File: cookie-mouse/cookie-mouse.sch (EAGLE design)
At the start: 8 parts

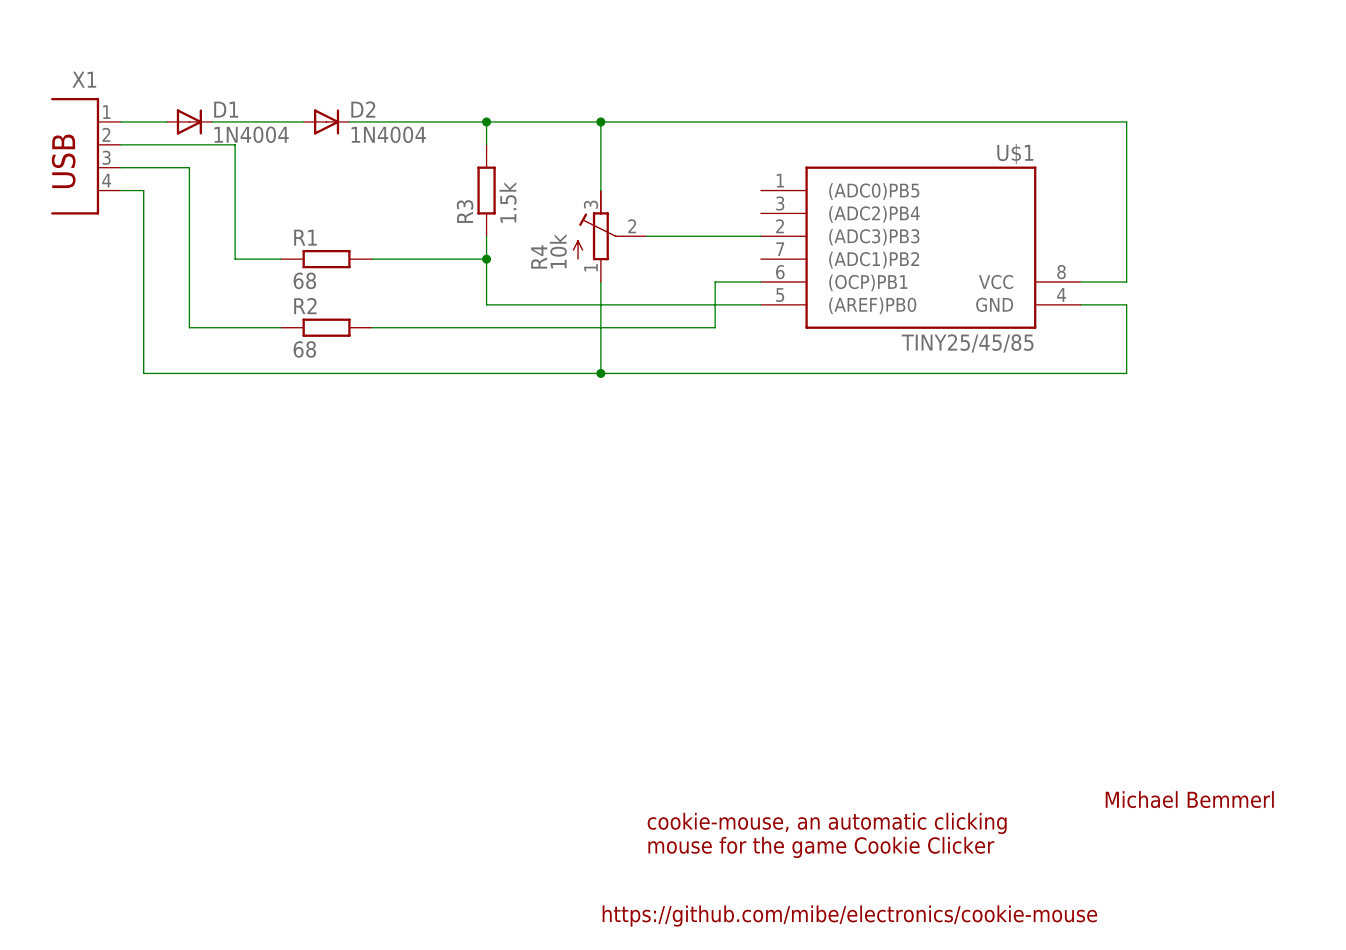
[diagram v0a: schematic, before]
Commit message: Added switch and push button, connected to ground.
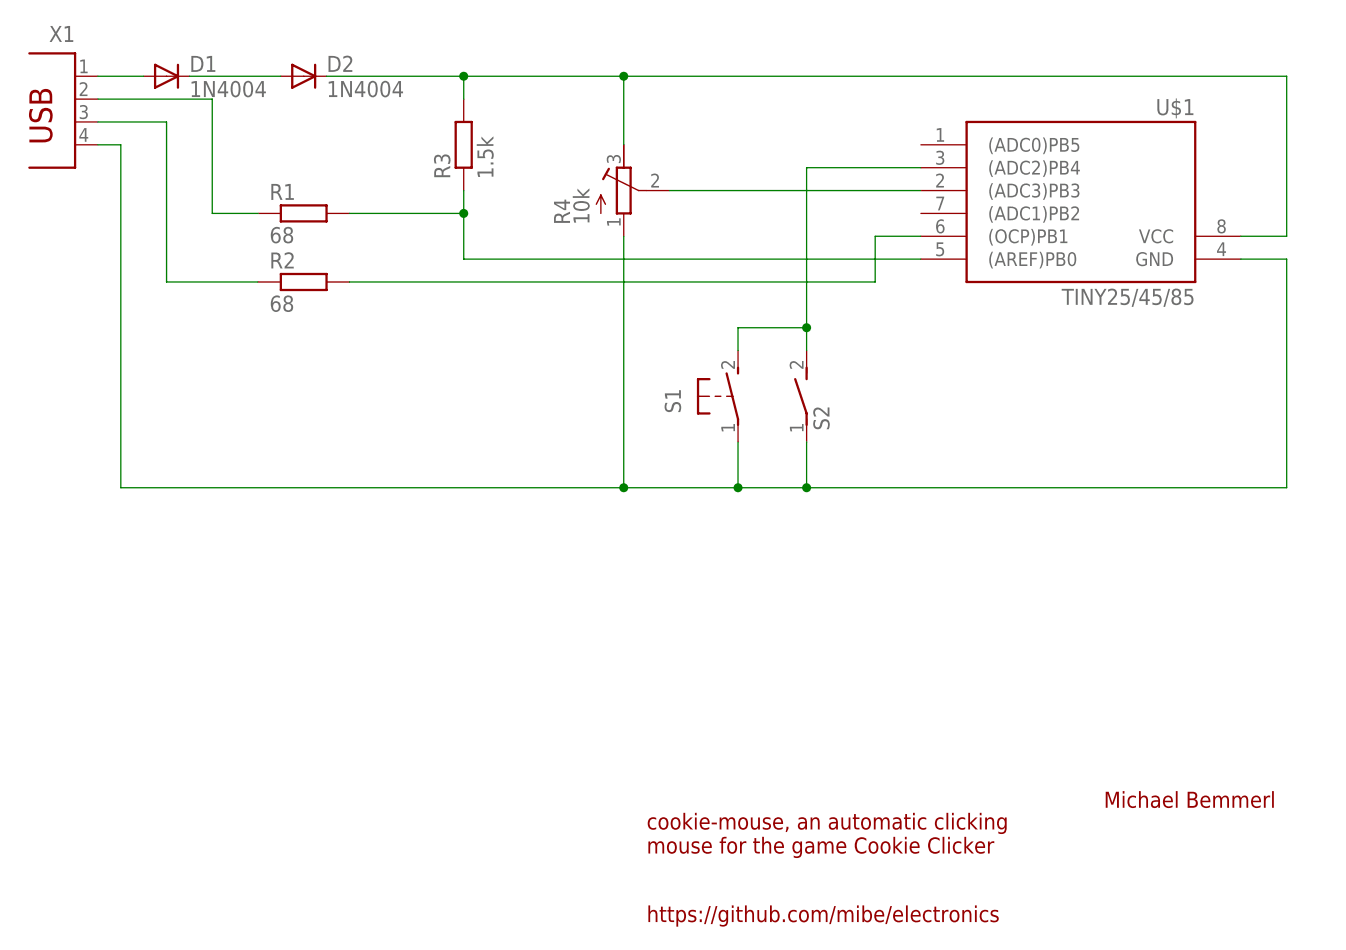
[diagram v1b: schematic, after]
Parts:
- added S1: (no value), switch-omron:31-XX
- added S2: (no value), switch-dil:DS01E
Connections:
- new net N$10: S1.S, S2.2, U$1.(ADC2)PB4
- net N$9: now also S1.P, S2.1
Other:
- note added: "https://github.com/mibe/electronics"
- note removed: "https://github.com/mibe/electronics/cookie-mouse"
- moved on the sheet: D1, D2, R1, R2, R3, R4, U$1, X1
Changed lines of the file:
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@@
 <part name="R3" library="resistor" deviceset="R-EU_" device="0207/10" value="1.5k"/>
 <part name="R4" library="resistor" deviceset="R-TRIMM" device="4G/J" value="10k"/>
+<part name="S1" library="switch-omron" deviceset="31-XX" device=""/>
+<part name="S2" library="switch-dil" deviceset="DS01E" device=""/>
 </parts>
 <sheets>
@@
 <text x="91.44" y="15.24" size="1.778" layer="94">cookie-mouse, an automatic clicking
 mouse for the game Cookie Clicker</text>
-<text x="86.36" y="7.62" size="1.778" layer="94">https://github.com/mibe/electronics/cookie-mouse</text>
+<text x="91.44" y="7.62" size="1.778" layer="94">https://github.com/mibe/electronics</text>
 </plain>
 <instances>
 <instance part="FRAME1" gate="G$1" x="0" y="0"/>
-<instance part="U$1" gate="G$1" x="121.92" y="81.28" rot="MR0"/>
-<instance part="X1" gate="G$1" x="30.48" y="91.44" rot="MR0"/>
-<instance part="D1" gate="1" x="40.64" y="96.52"/>
-<instance part="D2" gate="1" x="55.88" y="96.52"/>
-<instance part="R1" gate="G$1" x="55.88" y="81.28"/>
-<instance part="R2" gate="G$1" x="55.88" y="73.66"/>
-<instance part="R3" gate="G$1" x="73.66" y="88.9" rot="R90"/>
-<instance part="R4" gate="G$1" x="86.36" y="83.82"/>
+<instance part="U$1" gate="G$1" x="139.7" y="86.36" rot="MR0"/>
+<instance part="X1" gate="G$1" x="27.94" y="96.52" rot="MR0"/>
+<instance part="D1" gate="1" x="38.1" y="101.6"/>
+<instance part="D2" gate="1" x="53.34" y="101.6"/>
+<instance part="R1" gate="G$1" x="53.34" y="86.36"/>
+<instance part="R2" gate="G$1" x="53.34" y="78.74"/>
+<instance part="R3" gate="G$1" x="71.12" y="93.98" rot="R90"/>
+<instance part="R4" gate="G$1" x="88.9" y="88.9"/>
+<instance part="S1" gate="1" x="101.6" y="66.04"/>
+<instance part="S2" gate="1" x="109.22" y="66.04"/>
 </instances>
 <busses>
@@
 <pinref part="X1" gate="G$1" pin="1"/>
 <pinref part="D1" gate="1" pin="A"/>
-<wire x1="33.02" y1="96.52" x2="38.1" y2="96.52" width="0.1524" layer="91"/>
+<wire x1="30.48" y1="101.6" x2="35.56" y2="101.6" width="0.1524" layer="91"/>
 </segment>
 </net>
@@
 <pinref part="D1" gate="1" pin="C"/>
 <pinref part="D2" gate="1" pin="A"/>
-<wire x1="43.18" y1="96.52" x2="53.34" y2="96.52" width="0.1524" layer="91"/>
+<wire x1="40.64" y1="101.6" x2="50.8" y2="101.6" width="0.1524" layer="91"/>
 </segment>
 </net>
@@
 <segment>
 <pinref part="R1" gate="G$1" pin="1"/>
-<wire x1="50.8" y1="81.28" x2="45.72" y2="81.28" width="0.1524" layer="91"/>
+<wire x1="48.26" y1="86.36" x2="43.18" y2="86.36" width="0.1524" layer="91"/>
 <pinref part="X1" gate="G$1" pin="2"/>
-<wire x1="45.72" y1="81.28" x2="45.72" y2="93.98" width="0.1524" layer="91"/>
-<wire x1="45.72" y1="93.98" x2="33.02" y2="93.98" width="0.1524" layer="91"/>
+<wire x1="43.18" y1="86.36" x2="43.18" y2="99.06" width="0.1524" layer="91"/>
+<wire x1="43.18" y1="99.06" x2="30.48" y2="99.06" width="0.1524" layer="91"/>
 </segment>
 </net>
@@
 <segment>
 <pinref part="X1" gate="G$1" pin="3"/>
-<wire x1="33.02" y1="91.44" x2="40.64" y2="91.44" width="0.1524" layer="91"/>
-<wire x1="40.64" y1="91.44" x2="40.64" y2="73.66" width="0.1524" layer="91"/>
+<wire x1="30.48" y1="96.52" x2="38.1" y2="96.52" width="0.1524" layer="91"/>
+<wire x1="38.1" y1="96.52" x2="38.1" y2="78.74" width="0.1524" layer="91"/>
 <pinref part="R2" gate="G$1" pin="1"/>
-<wire x1="40.64" y1="73.66" x2="50.8" y2="73.66" width="0.1524" layer="91"/>
+<wire x1="38.1" y1="78.74" x2="48.26" y2="78.74" width="0.1524" layer="91"/>
 </segment>
 </net>
@@
 <segment>
 <pinref part="R1" gate="G$1" pin="2"/>
-<wire x1="60.96" y1="81.28" x2="73.66" y2="81.28" width="0.1524" layer="91"/>
+<wire x1="58.42" y1="86.36" x2="71.12" y2="86.36" width="0.1524" layer="91"/>
 <pinref part="R3" gate="G$1" pin="1"/>
-<wire x1="73.66" y1="81.28" x2="73.66" y2="83.82" width="0.1524" layer="91"/>
-<wire x1="73.66" y1="81.28" x2="73.66" y2="76.2" width="0.1524" layer="91"/>
-<wire x1="73.66" y1="76.2" x2="104.14" y2="76.2" width="0.1524" layer="91"/>
-<junction x="73.66" y="81.28"/>
+<wire x1="71.12" y1="86.36" x2="71.12" y2="88.9" width="0.1524" layer="91"/>
+<wire x1="71.12" y1="86.36" x2="71.12" y2="81.28" width="0.1524" layer="91"/>
+<wire x1="71.12" y1="81.28" x2="121.92" y2="81.28" width="0.1524" layer="91"/>
+<junction x="71.12" y="86.36"/>
 <pinref part="U$1" gate="G$1" pin="(AREF)PB0"/>
 </segment>
@@
 <segment>
 <pinref part="R3" gate="G$1" pin="2"/>
-<wire x1="73.66" y1="93.98" x2="73.66" y2="96.52" width="0.1524" layer="91"/>
-<wire x1="73.66" y1="96.52" x2="58.42" y2="96.52" width="0.1524" layer="91"/>
+<wire x1="71.12" y1="99.06" x2="71.12" y2="101.6" width="0.1524" layer="91"/>
+<wire x1="71.12" y1="101.6" x2="55.88" y2="101.6" width="0.1524" layer="91"/>
 <pinref part="D2" gate="1" pin="C"/>
-<wire x1="73.66" y1="96.52" x2="86.36" y2="96.52" width="0.1524" layer="91"/>
-<junction x="73.66" y="96.52"/>
-<wire x1="86.36" y1="96.52" x2="144.78" y2="96.52" width="0.1524" layer="91"/>
-<wire x1="144.78" y1="96.52" x2="144.78" y2="78.74" width="0.1524" layer="91"/>
+<wire x1="71.12" y1="101.6" x2="88.9" y2="101.6" width="0.1524" layer="91"/>
+<junction x="71.12" y="101.6"/>
+<wire x1="88.9" y1="101.6" x2="162.56" y2="101.6" width="0.1524" layer="91"/>
+<wire x1="162.56" y1="101.6" x2="162.56" y2="83.82" width="0.1524" layer="91"/>
 <pinref part="U$1" gate="G$1" pin="VCC"/>
-<wire x1="144.78" y1="78.74" x2="139.7" y2="78.74" width="0.1524" layer="91"/>
+<wire x1="162.56" y1="83.82" x2="157.48" y2="83.82" width="0.1524" layer="91"/>
 <pinref part="R4" gate="G$1" pin="A"/>
-<wire x1="86.36" y1="88.9" x2="86.36" y2="96.52" width="0.1524" layer="91"/>
-<junction x="86.36" y="96.52"/>
+<wire x1="88.9" y1="93.98" x2="88.9" y2="101.6" width="0.1524" layer="91"/>
+<junction x="88.9" y="101.6"/>
 </segment>
 </net>
@@
 <segment>
 <pinref part="R2" gate="G$1" pin="2"/>
-<wire x1="60.96" y1="73.66" x2="99.06" y2="73.66" width="0.1524" layer="91"/>
-<wire x1="99.06" y1="73.66" x2="99.06" y2="78.74" width="0.1524" layer="91"/>
+<wire x1="58.42" y1="78.74" x2="116.84" y2="78.74" width="0.1524" layer="91"/>
+<wire x1="116.84" y1="78.74" x2="116.84" y2="83.82" width="0.1524" layer="91"/>
 <pinref part="U$1" gate="G$1" pin="(OCP)PB1"/>
-<wire x1="99.06" y1="78.74" x2="104.14" y2="78.74" width="0.1524" layer="91"/>
+<wire x1="116.84" y1="83.82" x2="121.92" y2="83.82" width="0.1524" layer="91"/>
 </segment>
 </net>
@@
 <pinref part="R4" gate="G$1" pin="S"/>
 <pinref part="U$1" gate="G$1" pin="(ADC3)PB3"/>
-<wire x1="91.44" y1="83.82" x2="104.14" y2="83.82" width="0.1524" layer="91"/>
+<wire x1="93.98" y1="88.9" x2="121.92" y2="88.9" width="0.1524" layer="91"/>
 </segment>
 </net>
@@
 <segment>
 <pinref part="R4" gate="G$1" pin="E"/>
-<wire x1="86.36" y1="78.74" x2="86.36" y2="68.58" width="0.1524" layer="91"/>
+<wire x1="88.9" y1="83.82" x2="88.9" y2="55.88" width="0.1524" layer="91"/>
 <pinref part="X1" gate="G$1" pin="4"/>
-<wire x1="33.02" y1="88.9" x2="35.56" y2="88.9" width="0.1524" layer="91"/>
-<wire x1="35.56" y1="88.9" x2="35.56" y2="68.58" width="0.1524" layer="91"/>
-<wire x1="35.56" y1="68.58" x2="86.36" y2="68.58" width="0.1524" layer="91"/>
-<wire x1="86.36" y1="68.58" x2="144.78" y2="68.58" width="0.1524" layer="91"/>
-<junction x="86.36" y="68.58"/>
+<wire x1="30.48" y1="93.98" x2="33.02" y2="93.98" width="0.1524" layer="91"/>
+<wire x1="33.02" y1="93.98" x2="33.02" y2="55.88" width="0.1524" layer="91"/>
+<wire x1="33.02" y1="55.88" x2="88.9" y2="55.88" width="0.1524" layer="91"/>
+<wire x1="88.9" y1="55.88" x2="101.6" y2="55.88" width="0.1524" layer="91"/>
+<junction x="88.9" y="55.88"/>
 <pinref part="U$1" gate="G$1" pin="GND"/>
-<wire x1="144.78" y1="68.58" x2="144.78" y2="76.2" width="0.1524" layer="91"/>
-<wire x1="144.78" y1="76.2" x2="139.7" y2="76.2" width="0.1524" layer="91"/>
+<wire x1="101.6" y1="55.88" x2="109.22" y2="55.88" width="0.1524" layer="91"/>
+<wire x1="109.22" y1="55.88" x2="162.56" y2="55.88" width="0.1524" layer="91"/>
+<wire x1="162.56" y1="55.88" x2="162.56" y2="81.28" width="0.1524" layer="91"/>
+<wire x1="162.56" y1="81.28" x2="157.48" y2="81.28" width="0.1524" layer="91"/>
+<pinref part="S1" gate="1" pin="P"/>
+<wire x1="101.6" y1="60.96" x2="101.6" y2="55.88" width="0.1524" layer="91"/>
+<junction x="101.6" y="55.88"/>
+<pinref part="S2" gate="1" pin="1"/>
+<wire x1="109.22" y1="60.96" x2="109.22" y2="55.88" width="0.1524" layer="91"/>
+<junction x="109.22" y="55.88"/>
 </segment>
 </net>
+<net name="N$10" class="0">
+<segment>
+<pinref part="U$1" gate="G$1" pin="(ADC2)PB4"/>
+<pinref part="S2" gate="1" pin="2"/>
+<wire x1="121.92" y1="91.44" x2="109.22" y2="91.44" width="0.1524" layer="91"/>
+<wire x1="109.22" y1="91.44" x2="109.22" y2="73.66" width="0.1524" layer="91"/>
+<pinref part="S1" gate="1" pin="S"/>
+<wire x1="109.22" y1="73.66" x2="109.22" y2="71.12" width="0.1524" layer="91"/>
+<wire x1="101.6" y1="71.12" x2="101.6" y2="73.66" width="0.1524" layer="91"/>
+<wire x1="101.6" y1="73.66" x2="109.22" y2="73.66" width="0.1524" layer="91"/>
+<junction x="109.22" y="73.66"/>
+</segment>
+</net>
